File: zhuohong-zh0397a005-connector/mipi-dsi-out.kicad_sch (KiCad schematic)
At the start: 7 parts, among them J2 10051922-2010ELF, SW1 SMD-BUTTON_4P-5.2X5.2X1.5MM-S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

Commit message: Add LCSC numbers to C's and R's
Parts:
- C4: LCSC (none) -> C5189821
- C7, C8, C9: LCSC (none) -> C525264
- R1: LCSC (none) -> C2930027
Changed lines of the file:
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@@
+			)
+		)
+		(property "LCSC" "C525264"
+			(at 243.84 114.3 0)
+			(effects
+				(font
+					(size 1.27 1.27)
+				)
+				(hide yes)
 			)
 		)
@@
 			)
 		)
+		(property "LCSC" "C525264"
+			(at 256.54 114.3 0)
+			(effects
+				(font
+					(size 1.27 1.27)
+				)
+				(hide yes)
+			)
+		)
 		(pin "1"
 		)
@@
 			)
 		)
+		(property "LCSC" "C525264"
+			(at 231.14 114.3 0)
+			(effects
+				(font
+					(size 1.27 1.27)
+				)
+				(hide yes)
+			)
+		)
 		(pin "1"
 		)
@@
 			)
 		)
+		(property "LCSC" "C2930027"
+			(at 227.33 31.75 0)
+			(effects
+				(font
+					(size 1.27 1.27)
+				)
+				(hide yes)
+			)
+		)
 		(pin "2"
 		)
@@
 			(at 227.33 46.99 0)
 			(effects
+				(font
+					(size 1.27 1.27)
+				)
+				(hide yes)
+			)
+		)
+		(property "LCSC" "C5189821"
+			(at 227.33 46.99 0)
+			(effects

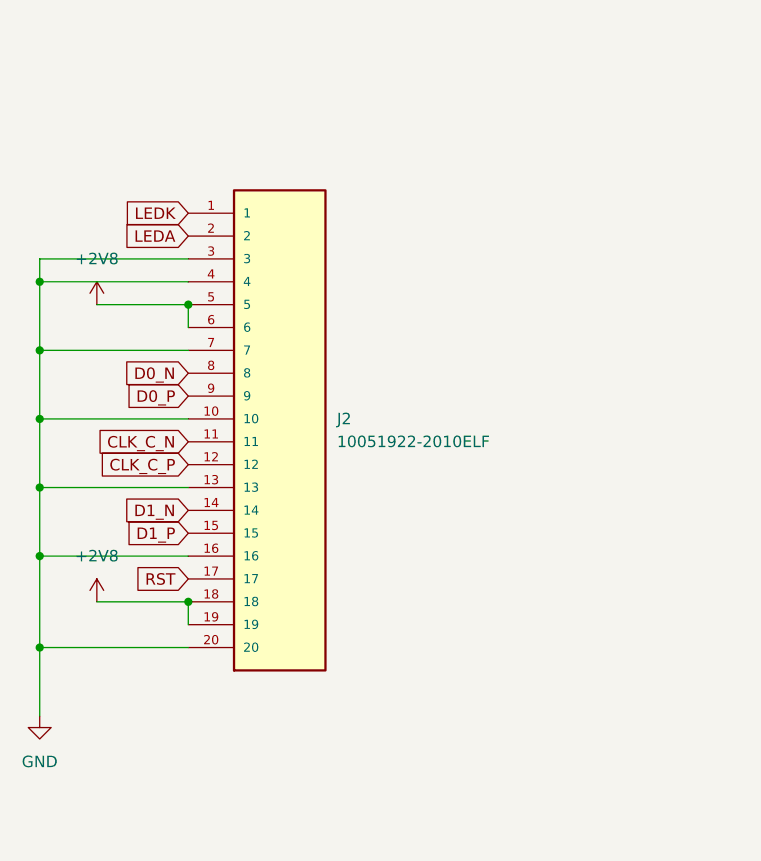
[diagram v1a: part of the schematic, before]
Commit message: Fixed lmt040wv004c board for production @ JLCPCB
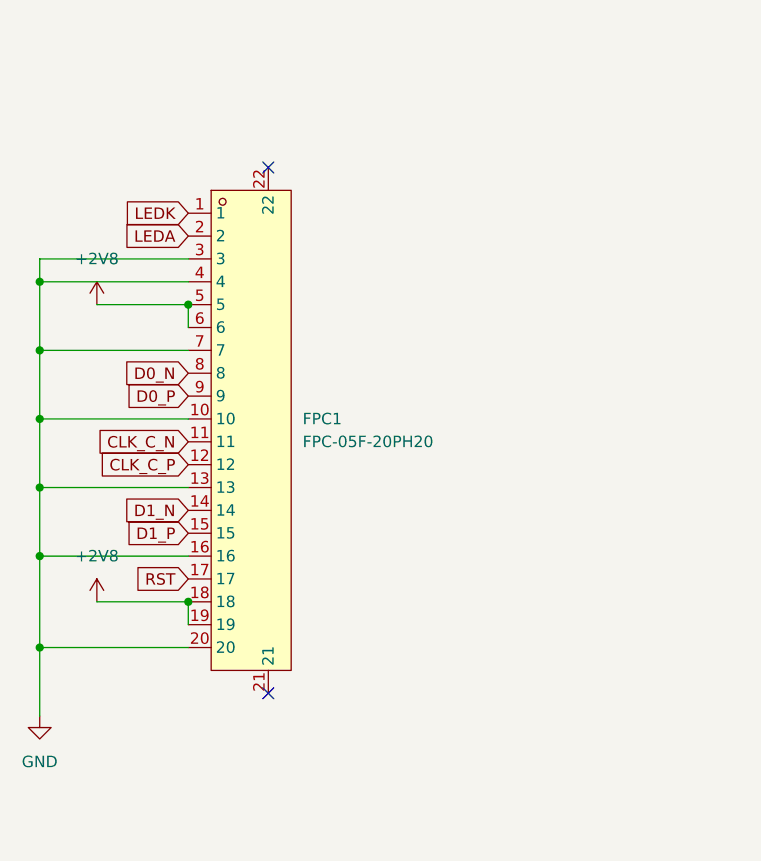
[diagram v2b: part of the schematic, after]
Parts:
- removed J2: 10051922-2010ELF, custom:AMPHENOL_10051922-2010ELF, symbol 10051922-2010ELF:10051922-2010ELF
- added FPC1: FPC-05F-20PH20, custom:FPC-SMD_20P-P0.50_XUNPU_FPC-05F-20PH20, symbol easyeda2kicad:FPC-05F-20PH20
- C4: LCSC C5189821 -> C386149
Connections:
- net +2V8: now also FPC1.18, FPC1.19, FPC1.5, FPC1.6
- net CLK_C_N: now also FPC1.11
- net CLK_C_P: now also FPC1.12
- net D0_N: now also FPC1.8
- net D0_P: now also FPC1.9
- net D1_N: now also FPC1.14
- net D1_P: now also FPC1.15
- net GND: now also FPC1.10, FPC1.13, FPC1.16, FPC1.20, FPC1.3, FPC1.4, FPC1.7
- net LEDA: now also FPC1.2
- net LEDK: now also FPC1.1
- net RST: now also FPC1.17
- no-connect marks 0 -> 2
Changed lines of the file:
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@@
+	)
+	(junction
+		(at 63.5 68.58)
+		(diameter 0)
+		(color 0 0 0 0)
+	)
+	(junction
+		(at 227.33 43.18)
+		(diameter 0)
+		(color 0 0 0 0)
+	)
+	(junction
+		(at 63.5 76.2)
+		(diameter 0)
+		(color 0 0 0 0)
+	)
+	(junction
+		(at 243.84 118.11)
+		(diameter 0)
+		(color 0 0 0 0)
+	)
+	(junction
+		(at 63.5 99.06)
+		(diameter 0)
+		(color 0 0 0 0)
+	)
+	(junction
+		(at 80.01 71.12)
+		(diameter 0)
+		(color 0 0 0 0)
 	)
 	(junction
@@
 	)
 	(junction
-		(at 63.5 68.58)
-		(diameter 0)
-		(color 0 0 0 0)
-	)
-	(junction
-		(at 227.33 43.18)
-		(diameter 0)
-		(color 0 0 0 0)
-	)
-	(junction
-		(at 63.5 76.2)
-		(diameter 0)
-		(color 0 0 0 0)
-	)
-	(junction
-		(at 243.84 118.11)
-		(diameter 0)
-		(color 0 0 0 0)
-	)
-	(junction
-		(at 80.01 71.12)
-		(diameter 0)
-		(color 0 0 0 0)
-	)
-	(junction
-		(at 63.5 99.06)
-		(diameter 0)
-		(color 0 0 0 0)
-	)
-	(junction
 		(at 231.14 118.11)
 		(diameter 0)
 		(color 0 0 0 0)
+	)
+	(no_connect
+		(at 88.9 114.3)
+	)
+	(no_connect
+		(at 88.9 55.88)
 	)
 	(wire
@@
 	)
 	(symbol
+		(lib_id "easyeda2kicad:FPC-05F-20PH20")
+		(at 86.36 86.36 0)
+		(unit 1)
+		(exclude_from_sim no)
+		(in_bom yes)
+		(on_board yes)
+		(dnp no)
+		(fields_autoplaced yes)
+		(property "Reference" "FPC1"
+			(at 92.71 83.8199 0)
+			(effects
+				(font
+					(size 1.27 1.27)
+				)
+				(justify left)
+			)
+		)
+		(property "Value" "FPC-05F-20PH20"
+			(at 92.71 86.3599 0)
+			(effects
+				(font
+					(size 1.27 1.27)
+				)
+				(justify left)
+			)
+		)
+		(property "Footprint" "custom:FPC-SMD_20P-P0.50_XUNPU_FPC-05F-20PH20"
+			(at 86.36 121.92 0)
+			(effects
+				(font
+					(size 1.27 1.27)
+				)
+				(hide yes)
+			)
+		)
+		(property "Datasheet" "https://datasheet.lcsc.com/lcsc/2109221030_XUNPU-FPC-05F-20PH20_C2856803.pdf"
+			(at 86.36 86.36 0)
+			(effects
+				(font
+					(size 1.27 1.27)
+				)
+				(hide yes)
+			)
+		)
+		(property "Description" "Right Angle 20P SMD,P=0.5mm"
+			(at 86.36 86.36 0)
+			(effects
+				(font
+					(size 1.27 1.27)
+				)
+				(hide yes)
+			)
+		)
+		(property "LCSC" "C2856803"
+			(at 86.36 124.46 0)
+			(effects
+				(font
+					(size 1.27 1.27)
+				)
+				(hide yes)
+			)
+		)
+		(pin "4"
+		)
+		(pin "22"
+		)
+		(pin "18"
+		)
+		(pin "6"
+		)
+		(pin "10"
+		)
+		(pin "21"
+		)
+		(pin "5"
+		)
+		(pin "16"
+		)
+		(pin "19"
+		)
+		(pin "17"
+		)
+		(pin "2"
+		)
+		(pin "3"
+		)
+		(pin "12"
+		)
+		(pin "8"
+		)
+		(pin "13"
+		)
+		(pin "7"
+		)
+		(pin "15"
+		)
+		(pin "14"
+		)
+		(pin "1"
+		)
+		(pin "9"
+		)
+		(pin "11"
+		)
+		(pin "20"
+		)
+		(instances
+			(project "50-24-fpc-adapter-board"
+				(path "/32028fb8-27d2-4a38-96f3-0c731f94a0fb/ea03a3c5-5ac0-4618-bb08-06acbdff3056"
+					(reference "FPC1")
+					(unit 1)
+				)
+			)
+		)
+	)
+	(symbol
 		(lib_id "Device:C")
 		(at 256.54 114.3 0)
@@
 				(path "/32028fb8-27d2-4a38-96f3-0c731f94a0fb/ea03a3c5-5ac0-4618-bb08-06acbdff3056"
 					(reference "R1")
-					(unit 1)
-				)
-			)
-		)
-	)
-	(symbol
-		(lib_id "10051922-2010ELF:10051922-2010ELF")
-		(at 90.17 83.82 0)
-		(unit 1)
-		(exclude_from_sim no)
-		(in_bom yes)
-		(on_board yes)
-		(dnp no)
-		(fields_autoplaced yes)
-		(property "Reference" "J2"
-			(at 96.52 83.8199 0)
-			(effects
-				(font
-					(size 1.27 1.27)
-				)
-				(justify left)
-			)
-		)
-		(property "Value" "10051922-2010ELF"
-			(at 96.52 86.3599 0)
-			(effects
-				(font
-					(size 1.27 1.27)
-				)
-				(justify left)
-			)
-		)
-		(property "Footprint" "custom:AMPHENOL_10051922-2010ELF"
-			(at 90.17 83.82 0)
-			(effects
-				(font
-					(size 1.27 1.27)
-				)
-				(justify bottom)
-				(hide yes)
-			)
-		)
-		(property "Datasheet" ""
-			(at 90.17 83.82 0)
-			(effects
-				(font
-					(size 1.27 1.27)
-				)
-				(hide yes)
-			)
-		)
-		(property "Description" ""
-			(at 90.17 83.82 0)
-			(effects
-				(font
-					(size 1.27 1.27)
-				)
-				(hide yes)
-			)
-		)
-		(property "MF" "Amphenol ICC"
-			(at 90.17 83.82 0)
-			(effects
-				(font
-					(size 1.27 1.27)
-				)
-				(justify bottom)
-				(hide yes)
-			)
-		)
-		(property "MAXIMUM_PACKAGE_HEIGHT" "3.37mm"
-			(at 90.17 83.82 0)
-			(effects
-				(font
-					(size 1.27 1.27)
-				)
-				(justify bottom)
-				(hide yes)
-			)
-		)
-		(property "Package" "None"
-			(at 90.17 83.82 0)
-			(effects
-				(font
-					(size 1.27 1.27)
-				)
-				(justify bottom)
-				(hide yes)
-			)
-		)
-		(property "Price" "None"
-			(at 90.17 83.82 0)
-			(effects
-				(font
-					(size 1.27 1.27)
-				)
-				(justify bottom)
-				(hide yes)
-			)
-		)
-		(property "Check_prices" "https://www.snapeda.com/parts/10051922-2010ELF/Amphenol+FCI/view-part/?ref=eda"
-			(at 90.17 83.82 0)
-			(effects
-				(font
-					(size 1.27 1.27)
-				)
-				(justify bottom)
-				(hide yes)
-			)
-		)
-		(property "STANDARD" "Manufacturer Recommendations"
-			(at 90.17 83.82 0)
-			(effects
-				(font
-					(size 1.27 1.27)
-				)
-				(justify bottom)
-				(hide yes)
-			)
-		)
-		(property "PARTREV" "K"
-			(at 90.17 83.82 0)
-			(effects
-				(font
-					(size 1.27 1.27)
-				)
-				(justify bottom)
-				(hide yes)
-			)
-		)
-		(property "SnapEDA_Link" "https://www.snapeda.com/parts/10051922-2010ELF/Amphenol+FCI/view-part/?ref=snap"
-			(at 90.17 83.82 0)
-			(effects
-				(font
-					(size 1.27 1.27)
-				)
-				(justify bottom)
-				(hide yes)
-			)
-		)
-		(property "MP" "10051922-2010ELF"
-			(at 90.17 83.82 0)
-			(effects
-				(font
-					(size 1.27 1.27)
-				)
-				(justify bottom)
-				(hide yes)
-			)
-		)
-		(property "Purchase-URL" "https://www.snapeda.com/api/url_track_click_mouser/?unipart_id=2873035&manufacturer=Amphenol ICC&part_name=10051922-2010ELF&search_term=None"
-			(at 90.17 83.82 0)
-			(effects
-				(font
-					(size 1.27 1.27)
-				)
-				(justify bottom)
-				(hide yes)
-			)
-		)
-		(property "Description_1" "\n0.50mm Flex Connector, VLL Series, 20 Position, Lower Side Contact, Side Entry Surface Mount ZIF Connector, Lead Free Type.\n"
-			(at 90.17 83.82 0)
-			(effects
-				(font
-					(size 1.27 1.27)
-				)
-				(justify bottom)
-				(hide yes)
-			)
-		)
-		(property "Availability" "In Stock"
-			(at 90.17 83.82 0)
-			(effects
-				(font
-					(size 1.27 1.27)
-				)
-				(justify bottom)
-				(hide yes)
-			)
-		)
-		(property "MANUFACTURER" "Amphenol"
-			(at 90.17 83.82 0)
-			(effects
-				(font
-					(size 1.27 1.27)
-				)
-				(justify bottom)
-				(hide yes)
-			)
-		)
-		(property "LCSC" "C3169799"
-			(at 90.17 83.82 0)
-			(effects
-				(font
-					(size 1.27 1.27)
-				)
-				(hide yes)
-			)
-		)
-		(pin "12"
-		)
-		(pin "13"
-		)
-		(pin "14"
-		)
-		(pin "15"
-		)
-		(pin "3"
-		)
-		(pin "9"
-		)
-		(pin "2"
-		)
-		(pin "18"
-		)
-		(pin "17"
-		)
-		(pin "20"
-		)
-		(pin "16"
-		)
-		(pin "10"
-		)
-		(pin "8"
-		)
-		(pin "1"
-		)
-		(pin "19"
-		)
-		(pin "11"
-		)
-		(pin "5"
-		)
-		(pin "7"
-		)
-		(pin "4"
-		)
-		(pin "6"
-		)
-		(instances
-			(project "50-24-fpc-adapter-board"
-				(path "/32028fb8-27d2-4a38-96f3-0c731f94a0fb/ea03a3c5-5ac0-4618-bb08-06acbdff3056"
-					(reference "J2")
 					(unit 1)
 				)
@@
 			)
 		)
-		(property "LCSC" "C5189821"
+		(property "LCSC" "C386149 "
 			(at 227.33 46.99 0)
 			(effects
